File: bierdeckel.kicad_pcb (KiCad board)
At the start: 2 copper layers, 93 x 93 mm, 67 parts, among them IC1 HSFPAR004A, J1 Pogo, J2 Pogo, J6 USB4110-GF-A, Q1 BSS138P,215, SW1 PTS526 SK15 SMTR2 LFS, SW2 PTS526 SK15 SMTR2 LFS, SW3 PTS526 SK15 SMTR2 LFS, U1 ESP32-C3-WROOM-02, U2 BQ25176J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

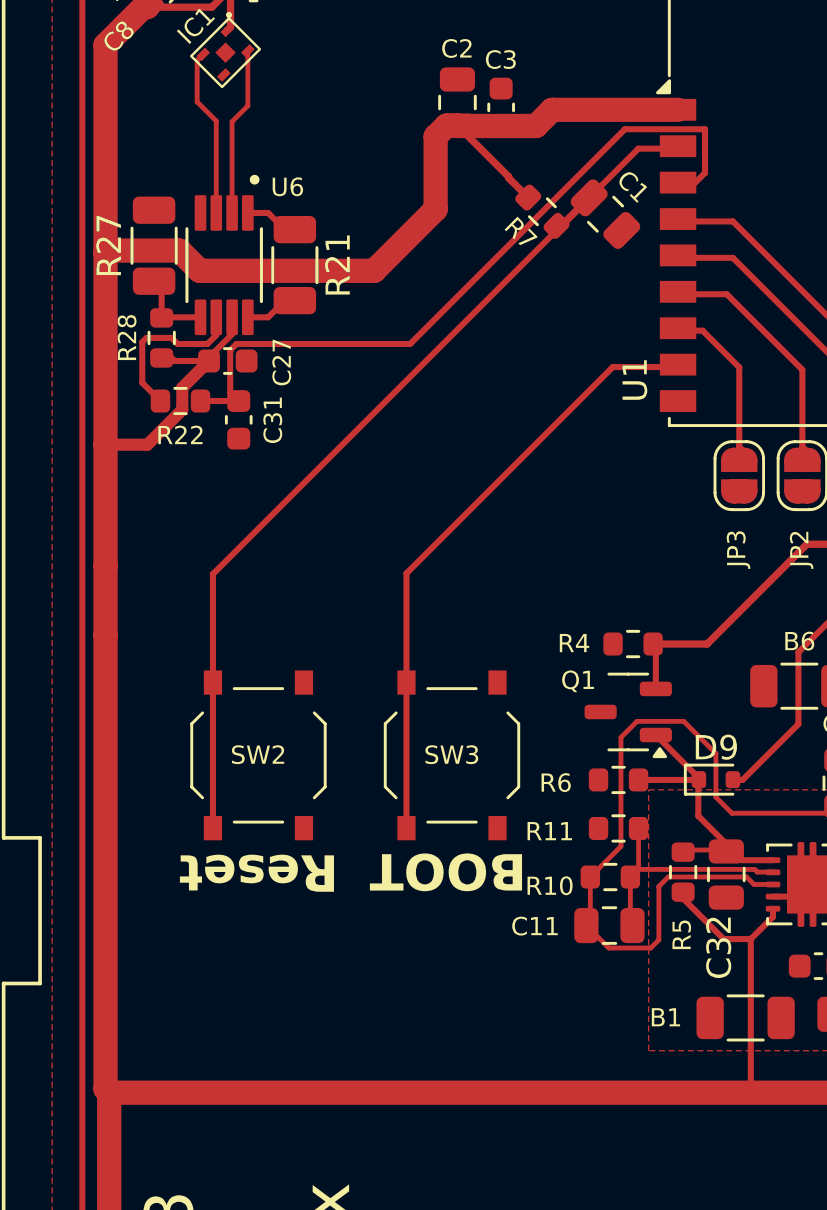
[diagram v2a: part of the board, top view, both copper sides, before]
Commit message: reposition buttons and finish up initial base design
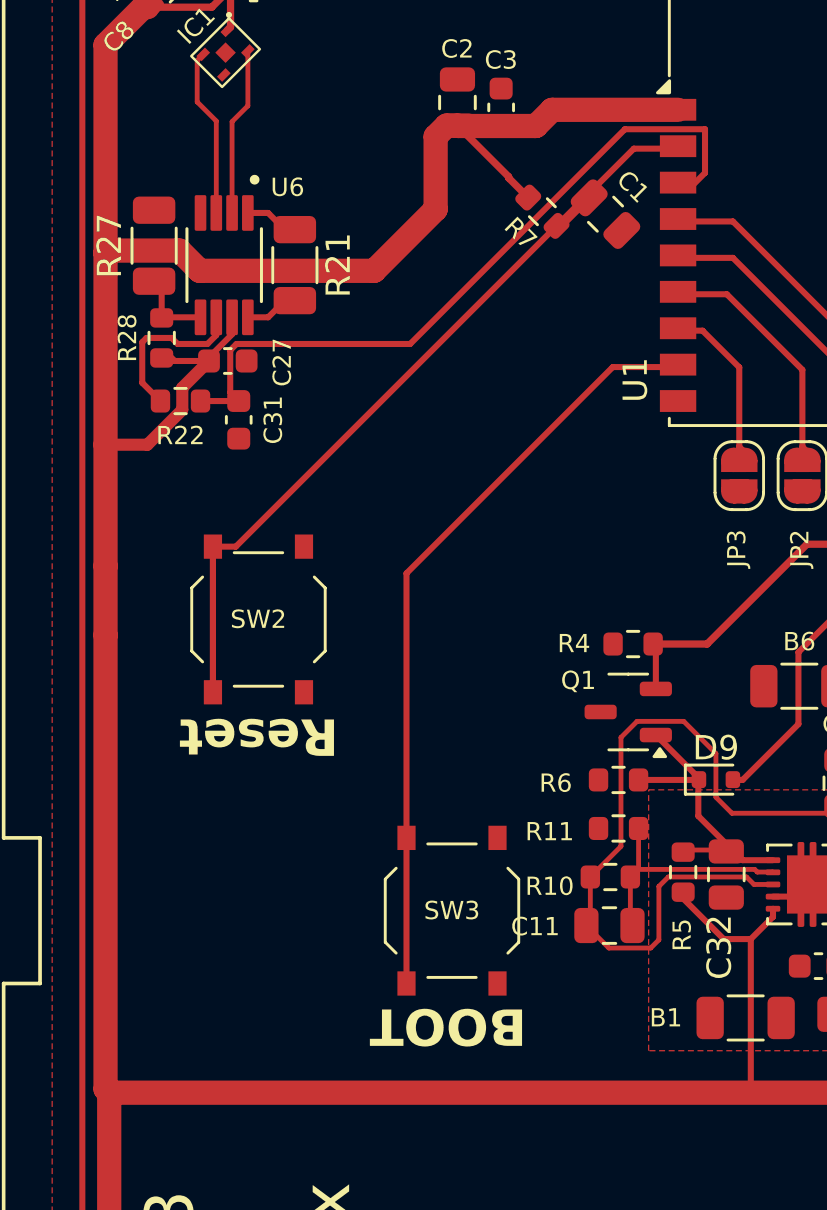
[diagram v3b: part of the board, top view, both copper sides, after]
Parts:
- D6: value 150060BS73220 -> XL-1608UBC-04
- D7: value 150060GS73220 -> A-SP192DGHC-C01-4T
- J6: value USB4110-GF-A -> USB-TYPE-C-020
- moved SW3 6.40 mm to (120.5, 96.5)
- moved SW2 5.60 mm to (112.5, 84.5)
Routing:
- net /~{BOOTLOADER}: track 25.2 -> 31.6 mm
- net /RST: track 39.0 -> 39.6 mm
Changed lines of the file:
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@@
 	(footprint "Button_Switch_SMD:SW_Push_1P1T_XKB_TS-1187A"
 		(layer "F.Cu")
-		(at 120.475 90.1 -90)
+		(at 120.475 96.5 -90)
 		(descr "SMD Tactile Switch, http://www.helloxkb.com/public/images/pdf/TS-1187A-X-X-X.pdf")
 		(tags "SPST Tactile Switch")
@@
 			)
 		)
-		(property "Value" "150060GS73220"
+		(property "Value" "A-SP192DGHC-C01-4T"
 			(at 0 1.43 0)
 			(layer "F.Fab")
@@
 			)
 		)
-		(property "mpn" "A-SP192DGHC-C01-4T"
+		(property "mpn" "C19171301"
 			(at 0 0 0)
 			(layer "F.Fab")
@@
 			)
 		)
-		(property "part#" "150060GS73220"
+		(property "part#" "C19171301"
 			(at 0 0 0)
 			(layer "F.Fab")
@@
 			)
 		)
-		(property "Value" "USB4110-GF-A"
+		(property "Value" "USB-TYPE-C-020"
 			(at 0 5 180)
 			(unlocked yes)
@@
 			)
 		)
-		(property "mpn" "USB4110-GF-A"
+		(property "mpn" "C2927040"
 			(at 0 0 180)
 			(unlocked yes)
@@
 	(footprint "Button_Switch_SMD:SW_Push_1P1T_XKB_TS-1187A"
 		(layer "F.Cu")
-		(at 112.5 90.1 -90)
+		(at 112.5 84.5 -90)
 		(descr "SMD Tactile Switch, http://www.helloxkb.com/public/images/pdf/TS-1187A-X-X-X.pdf")
 		(tags "SPST Tactile Switch")
@@
 			)
 		)
-		(property "Value" "150060BS73220"
+		(property "Value" "XL-1608UBC-04"
 			(at 0 1.43 90)
 			(layer "F.Fab")
@@
 			)
 		)
-		(property "mpn" "XL-1608UBC-04"
+		(property "mpn" "C965807"
 			(at 0 0 0)
 			(layer "F.Fab")
@@
 			)
 		)
-		(property "part#" "150060BS73220"
+		(property "part#" "C965807"
 			(at 0 0 0)
 			(layer "F.Fab")
@@
 	)
 	(gr_text "Reset"
-		(at 115.8 94.0375 180)
+		(at 115.8 88.4375 180)
 		(layer "F.SilkS")
 		(effects
@@
 	)
 	(gr_text "BOOT"
-		(at 123.55 93.9875 180)
+		(at 123.55 100.3875 180)
 		(layer "F.SilkS")
 		(effects
@@
 	)
 	(gr_text_box "lipo 34x50"
-		(locked yes)
-		(start 123 105)
-		(end 173 139)
+		(start 121.5 107)
+		(end 171.5 141)
 		(margins 0.825 0.825 0.825 0.825)
 		(layer "F.SilkS")
@@
 	)
 	(segment
+		(start 111.566726 81.5)
+		(end 127.966726 65.1)
+		(width 0.25)
+		(layer "F.Cu")
+		(net 5)
+	)
+	(segment
 		(start 124.783363 68.283363)
 		(end 124.973135 68.283363)
@@
 	)
 	(segment
-		(start 110.625 93.1)
-		(end 110.625 87.1)
+		(start 110.625 87.1)
+		(end 110.625 81.5)
 		(width 0.25)
 		(layer "F.Cu")
@@
 	)
 	(segment
-		(start 110.625 87.1)
-		(end 110.625 82.631498)
+		(start 110.625 87.5)
+		(end 110.625 81.5)
 		(width 0.25)
 		(layer "F.Cu")
@@
 	)
 	(segment
-		(start 128.156498 65.1)
-		(end 129.79 65.1)
+		(start 110.625 81.5)
+		(end 111.566726 81.5)
 		(width 0.25)
 		(layer "F.Cu")
@@
 	)
 	(segment
-		(start 110.625 82.631498)
-		(end 128.156498 65.1)
+		(start 127.966726 65.1)
+		(end 129.79 65.1)
 		(width 0.25)
 		(layer "F.Cu")
@@
 	)
 	(segment
-		(start 118.6 87.1)
+		(start 127.1 74.1)
 		(end 118.6 82.6)
 		(width 0.25)
@@
 	)
 	(segment
-		(start 118.6 82.6)
-		(end 127.1 74.1)
+		(start 118.6 99.5)
+		(end 118.6 93.5)
 		(width 0.25)
 		(layer "F.Cu")
@@
 	)
 	(segment
-		(start 127.1 74.1)
-		(end 129.79 74.1)
+		(start 129.79 74.1)
+		(end 127.1 74.1)
 		(width 0.25)
 		(layer "F.Cu")
@@
 	)
 	(segment
-		(start 118.6 93.1)
-		(end 118.6 87.1)
+		(start 118.6 82.6)
+		(end 118.6 93.5)
 		(width 0.25)
 		(layer "F.Cu")

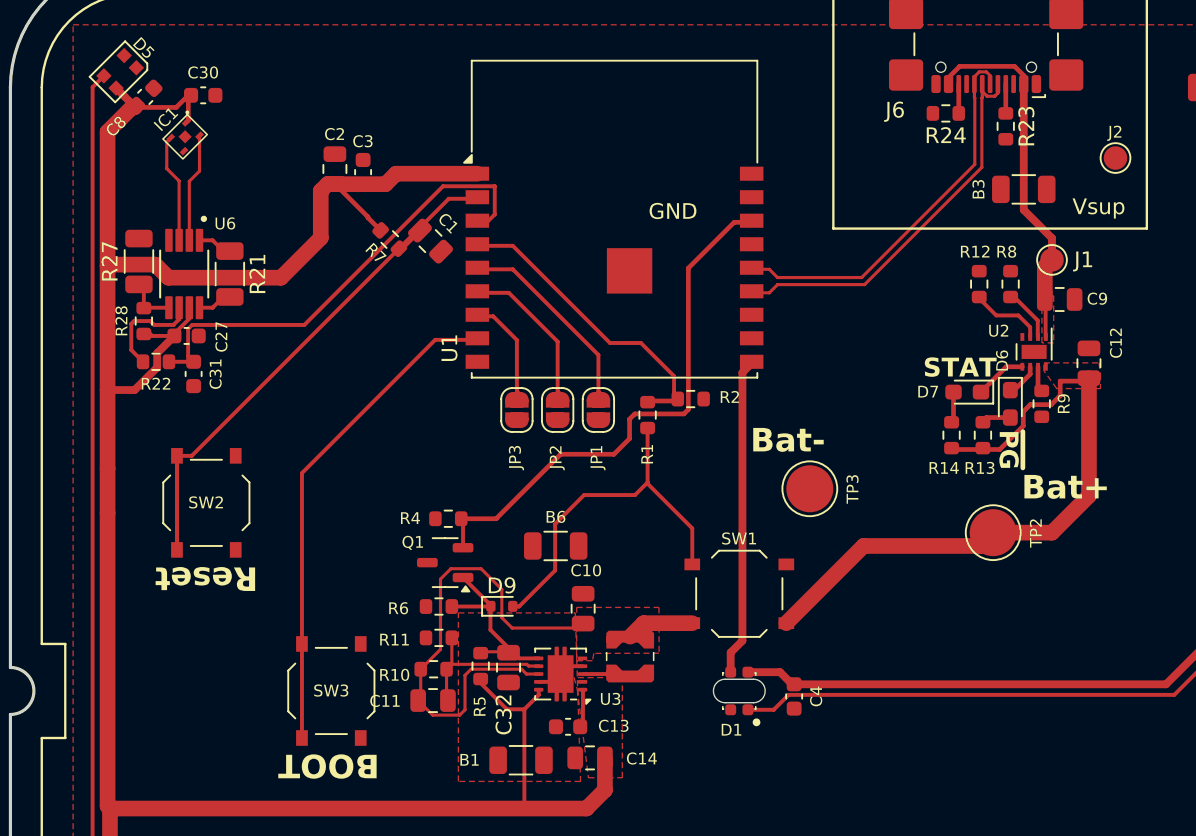
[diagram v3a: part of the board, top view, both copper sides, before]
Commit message: route power latch circuit
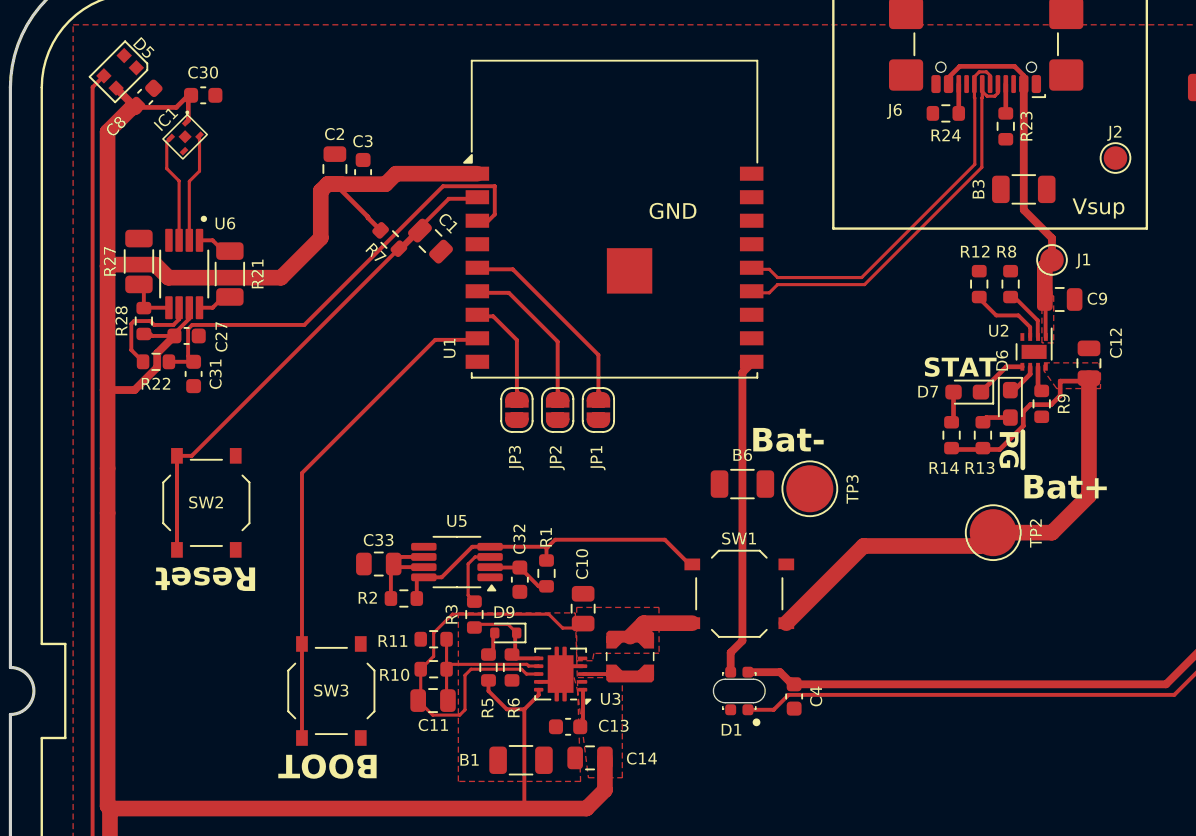
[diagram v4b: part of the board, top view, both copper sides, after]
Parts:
- removed Q1: BSS138P,215, Package_TO_SOT_SMD:SOT-23-3
- removed R4: 200k, Resistor_SMD:R_0603_1608Metric
- added C33: 10u, Capacitor_SMD:C_0805_2012Metric, F.Cu at (123.5, 88.4)
- added R3: 620, Resistor_SMD:R_0603_1608Metric, F.Cu at (129.6, 91.6)
- added U5: LMC555xMM, Package_SO:VSSOP-8_3x3mm_P0.65mm, F.Cu at (128.5, 88.3)
- C32: value 1uF -> 0.1uF; footprint Capacitor_SMD:C_0805_2012Metric -> Capacitor_SMD:C_0603_1608Metric
- R1: value 200k -> 620
- R5: value 200k -> 10k
- moved R2 22.3 mm to (125.1, 90.6), turned to 0 degrees
- moved B6 12.6 mm to (146.7, 83.3)
- moved R1 12.0 mm to (134.2, 89.0), turned to 90 degrees
- moved R6 6.07 mm to (132.0, 95.0), turned to -90 degrees
- moved C32 5.66 mm to (132.5, 89.4)
- moved D9 1.72 mm to (131.6, 92.8), turned to 180 degrees
- moved R5 0.51 mm to (130.5, 95.0)
- moved R11 0.35 mm to (127.0, 93.2)
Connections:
- C32 pad 1: /PSU_EN -> Net-(U5-TR)
- R1 pad 1: /PSU_EN_SENSE -> Net-(U5-TR)
- R1 pad 2: Net-(D9-A) -> Net-(U5-R)
- R2 pad 1: GND -> Net-(U5-DIS)
- R2 pad 2: /PSU_EN_SENSE -> Net-(U5-R)
- R5 pad 1: /PSU_EN -> Net-(D9-A)
- SW1 pad 2: Net-(D9-A) -> Net-(U5-R)
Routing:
- net /PWR_OFF: track 34.1 -> 0.00 mm
- net Net-(D9-A): track 23.5 -> 1.54 mm
- net Net-(U5-R): track 0.00 -> 21.5 mm
- net /PSU_EN_SENSE: track 19.4 -> 0.00 mm
- net Net-(U5-DIS): track 0.00 -> 6.39 mm
- net /PSU_EN: track 12.3 -> 6.31 mm
- net +BATT: track 77.3 -> 72.1 mm
- net Net-(U5-Q): track 0.00 -> 4.15 mm
- net Net-(U5-TR): track 0.00 -> 4.11 mm

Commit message: prepare for ordering
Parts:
- added R4: 10k, Resistor_SMD:R_0603_1608Metric, F.Cu at (134.2, 86.0)
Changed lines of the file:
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@@
 			(net 33 "/PSU_EN_SENSE")
 			(pinfunction "IO5")
-			(pintype "bidirectional")
+			(pintype "bidirectional+no_connect")
 		)
 		(pad "5" smd rect
@@
 			(net 12 "/PWR_OFF")
 			(pinfunction "IO2")
-			(pintype "bidirectional")
+			(pintype "bidirectional+no_connect")
 		)
 		(pad "17" smd rect
@@
 		(embedded_fonts no)
 	)
+	(footprint "Resistor_SMD:R_0603_1608Metric"
+		(layer "F.Cu")
+		(at 134.2 85.975 -90)
+		(descr "Resistor SMD 0603 (1608 Metric), square (rectangular) end terminal, IPC-7351 nominal, (Body size source: IPC-SM-782 page 72, https://www.pcb-3d.com/wordpress/wp-content/uploads/ipc-sm-782a_amendment_1_and_2.pdf), generated with kicad-footprint-generator")
+		(tags "resistor")
+		(property "Reference" "R4"
+			(at 0 -1.43 90)
+			(layer "F.SilkS")
+			(effects
+				(font
+					(size 0.75 0.75)
+					(thickness 0.15)
+				)
+			)
+		)
+		(property "Value" "10k"
+			(at 0 1.43 90)
+			(layer "F.Fab")
+			(effects
+				(font
+					(size 1 1)
+					(thickness 0.15)
+				)
+			)
+		)
+		(property "Datasheet" "~"
+			(at 0 0 90)
+			(layer "F.Fab")
+			(hide yes)
+			(effects
+				(font
+					(size 1.27 1.27)
+					(thickness 0.15)
+				)
+			)
+		)
+		(property "Description" "Resistor"
+			(at 0 0 90)
+			(layer "F.Fab")
+			(hide yes)
+			(effects
+				(font
+					(size 1.27 1.27)
+					(thickness 0.15)
+				)
+			)
+		)
+		(property "mpn" ""
+			(at 0 0 270)
+			(unlocked yes)
+			(layer "F.Fab")
+			(hide yes)
+			(effects
+				(font
+					(size 1 1)
+					(thickness 0.15)
+				)
+			)
+		)
+		(property ki_fp_filters "R_*")
+		(sheetname "/")
+		(sheetfile "bierdeckel.kicad_sch")
+		(attr smd dnp)
+		(fp_line
+			(start -0.237258 0.5225)
+			(end 0.237258 0.5225)
+			(stroke
+				(width 0.12)
+				(type solid)
+			)
+			(layer "F.SilkS")
+		)
+		(fp_line
+			(start -0.237258 -0.5225)
+			(end 0.237258 -0.5225)
+			(stroke
+				(width 0.12)
+				(type solid)
+			)
+			(layer "F.SilkS")
+		)
+		(fp_line
+			(start -1.48 0.73)
+			(end -1.48 -0.73)
+			(stroke
+				(width 0.05)
+				(type solid)
+			)
+			(layer "F.CrtYd")
+		)
+		(fp_line
+			(start 1.48 0.73)
+			(end -1.48 0.73)
+			(stroke
+				(width 0.05)
+				(type solid)
+			)
+			(layer "F.CrtYd")
+		)
+		(fp_line
+			(start -1.48 -0.73)
+			(end 1.48 -0.73)
+			(stroke
+				(width 0.05)
+				(type solid)
+			)
+			(layer "F.CrtYd")
+		)
+		(fp_line
+			(start 1.48 -0.73)
+			(end 1.48 0.73)
+			(stroke
+				(width 0.05)
+				(type solid)
+			)
+			(layer "F.CrtYd")
+		)
+		(fp_line
+			(start -0.8 0.4125)
+			(end -0.8 -0.4125)
+			(stroke
+				(width 0.1)
+				(type solid)
+			)
+			(layer "F.Fab")
+		)
+		(fp_line
+			(start 0.8 0.4125)
+			(end -0.8 0.4125)
+			(stroke
+				(width 0.1)
+				(type solid)
+			)
+			(layer "F.Fab")
+		)
+		(fp_line
+			(start -0.8 -0.4125)
+			(end 0.8 -0.4125)
+			(stroke
+				(width 0.1)
+				(type solid)
+			)
+			(layer "F.Fab")
+		)
+		(fp_line
+			(start 0.8 -0.4125)
+			(end 0.8 0.4125)
+			(stroke
+				(width 0.1)
+				(type solid)
+			)
+			(layer "F.Fab")
+		)
+		(fp_text user "${REFERENCE}"
+			(at 0 0 90)
+			(layer "F.Fab")
+			(effects
+				(font
+					(size 0.4 0.4)
+					(thickness 0.06)
+				)
+			)
+		)
+		(pad "1" smd roundrect
+			(at -0.825 0 270)
+			(size 0.8 0.95)
+			(layers "F.Cu" "F.Mask" "F.Paste")
+			(roundrect_rratio 0.25)
+			(net 1 "GND")
+			(pintype "passive")
+		)
+		(pad "2" smd roundrect
+			(at 0.825 0 270)
+			(size 0.8 0.95)
+			(layers "F.Cu" "F.Mask" "F.Paste")
+			(roundrect_rratio 0.25)
+			(net 50 "Net-(U5-R)")
+			(pintype "passive")
+		)
+		(embedded_fonts no)
+		(model "${KICAD9_3DMODEL_DIR}/Resistor_SMD.3dshapes/R_0603_1608Metric.step"
+			(offset
+				(xyz 0 0 0)
+			)
+			(scale
+				(xyz 1 1 1)
+			)
+			(rotate
+				(xyz 0 0 0)
+			)
+		)
+	)
 	(footprint "Capacitor_SMD:C_0603_1608Metric"
 		(layer "F.Cu")
@@
 		(tags "resistor")
 		(property "Reference" "R1"
-			(at 2.3 0 270)
+			(at 0.2 1.3 270)
 			(layer "F.SilkS")
 			(effects
@@
 			(net 1 "GND")
 			(pinfunction "V_")
-			(pintype "bidirectional")
+			(pintype "power_in")
 		)
 		(pad "5" smd roundrect
@@
 			(pinfunction "VAUX")
 			(pintype "bidirectional")
-			(solder_mask_margin 0.07)
 			(solder_paste_margin -0.025)
 		)
@@
 			(pinfunction "VOUT")
 			(pintype "power_out")
-			(solder_mask_margin 0.07)
 			(solder_paste_margin -0.025)
 		)
@@
 			(pinfunction "L")
 			(pintype "input")
-			(solder_mask_margin 0.07)
 			(solder_paste_margin -0.025)
 		)
@@
 			(pinfunction "PGND")
 			(pintype "power_in")
-			(solder_mask_margin 0.07)
 			(solder_paste_margin -0.025)
 		)
@@
 			(pinfunction "VIN")
 			(pintype "power_in")
-			(solder_mask_margin 0.07)
 			(solder_paste_margin -0.025)
 		)
@@
 			(pinfunction "EN")
 			(pintype "input")
-			(solder_mask_margin 0.07)
 			(solder_paste_margin -0.025)
 		)
@@
 			(pinfunction "UVLO")
 			(pintype "input")
-			(solder_mask_margin 0.07)
 			(solder_paste_margin -0.025)
 		)
@@
 			(pinfunction "PS")
 			(pintype "input")
-			(solder_mask_margin 0.07)
 			(solder_paste_margin -0.025)
 		)
@@
 			(pinfunction "GND")
 			(pintype "power_in")
-			(solder_mask_margin 0.07)
 			(solder_paste_margin -0.025)
 		)
@@
 			(pinfunction "FB")
 			(pintype "input")
-			(solder_mask_margin 0.07)
 			(solder_paste_margin -0.025)
 		)
@@
 	)
 	(segment
-		(start 134.3 87.3)
-		(end 130.6 87.3)
+		(start 134.2 88.175)
+		(end 134.2 86.8)
 		(width 0.25)
 		(layer "F.Cu")
@@
 	)
 	(segment
-		(start 143.325 88.425)
-		(end 141.75 86.85)
+		(start 134.2 86.8)
+		(end 133.7 87.3)
 		(width 0.25)
 		(layer "F.Cu")
@@
 	)
 	(segment
-		(start 125.925 89.25)
-		(end 126.375 89.25)
+		(start 143.5 88.425)
+		(end 143.325 88.425)
 		(width 0.25)
 		(layer "F.Cu")
@@
 	)
 	(segment
-		(start 143.5 88.425)
-		(end 143.325 88.425)
+		(start 125.925 89.25)
+		(end 126.375 89.25)
 		(width 0.25)
 		(layer "F.Cu")
@@
 	)
 	(segment
-		(start 125.925 90.6)
-		(end 125.925 89.25)
+		(start 143.325 88.425)
+		(end 141.75 86.85)
 		(width 0.25)
 		(layer "F.Cu")
@@
 	)
 	(segment
-		(start 141.75 86.85)
-		(end 134.75 86.85)
+		(start 125.925 90.6)
+		(end 125.925 89.25)
 		(width 0.25)
 		(layer "F.Cu")
@@
 	)
 	(segment
-		(start 134.2 87.4)
-		(end 134.3 87.3)
+		(start 134.25 86.85)
+		(end 134.2 86.8)
 		(width 0.25)
 		(layer "F.Cu")
@@
 	)
 	(segment
-		(start 134.2 88.175)
-		(end 134.2 87.4)
+		(start 127.5125 89.25)
+		(end 129.4625 87.3)
 		(width 0.25)
 		(layer "F.Cu")
@@
 	)
 	(segment
-		(start 127.5125 89.25)
-		(end 129.4625 87.3)
+		(start 133.7 87.3)
+		(end 130.6 87.3)
 		(width 0.25)
 		(layer "F.Cu")
@@
 	)
 	(segment
-		(start 134.75 86.85)
-		(end 134.3 87.3)
+		(start 141.75 86.85)
+		(end 134.25 86.85)
 		(width 0.25)
 		(layer "F.Cu")

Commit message: add unit to capacitor value
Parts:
- C33: value 10u -> 10uF
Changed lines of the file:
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@@
 			)
 		)
-		(property "Value" "10u"
+		(property "Value" "10uF"
 			(at 0 1.68 0)
 			(layer "F.Fab")
